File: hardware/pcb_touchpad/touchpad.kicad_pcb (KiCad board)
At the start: 2 copper layers, 41.3 x 30.3 mm, 24 parts, among them U1 IQS9151

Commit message: assigned correct nets to vias
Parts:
- moved U1 32.3 mm to (202.0, 89.7)
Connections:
- net Net-(U1-RX0/TX0) renamed /COL10
- net Net-(U1-RX11/TX11) renamed /ROW13
- net Net-(U1-RX12/TX12) renamed /ROW12
- net Net-(U1-RX1/TX1) renamed /COL9
- net Net-(U1-RX2/TX2) renamed /COL8
- net Net-(U1-RX3/TX3) renamed /COL7
- net Net-(U1-RX4/TX4) renamed /COL6
- net Net-(U1-RX5/TX5) renamed /COL5
- net Net-(U1-RX6/TX6) renamed /COL4
- net Net-(U1-RX7/TX7) renamed /COL3
- net Net-(U1-RX8/TX8) renamed /COL2
- net Net-(U1-RX9/TX9) renamed /COL1
- net Net-(U1-TX33) renamed /ROW11
- net Net-(U1-TX34) renamed /ROW10
- net Net-(U1-TX35) renamed /ROW9
- net Net-(U1-TX36) renamed /ROW8
- net Net-(U1-TX37) renamed /ROW
- net Net-(U1-TX38) renamed /ROW6
- net Net-(U1-TX39) renamed /ROW5
- net Net-(U1-TX40) renamed /ROW4
- net Net-(U1-TX41) renamed /ROW3
- net Net-(U1-TX42) renamed /ROW2
- net Net-(U1-TX43) renamed /ROW1
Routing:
- net (no net): track 141.8 -> 0.00 mm, vias 234 -> 0
- net /COL7: track 0.00 -> 15.8 mm, vias 0 -> 26
- net /COL6: track 0.00 -> 15.8 mm, vias 0 -> 26
- net /COL5: track 0.00 -> 15.8 mm, vias 0 -> 26
- net /COL4: track 0.00 -> 15.8 mm, vias 0 -> 26
- net /COL3: track 0.00 -> 15.8 mm, vias 0 -> 26
- net /COL10: track 0.00 -> 15.8 mm, vias 0 -> 26
- net /COL1: track 0.00 -> 15.8 mm, vias 0 -> 26
- net /COL9: track 1.21 -> 15.8 mm, vias 2 -> 26
- net /COL8: track 1.21 -> 15.8 mm, vias 2 -> 26
- net /COL2: track 1.21 -> 15.8 mm, vias 2 -> 26
- net GND: track 6.06 -> 0.00 mm, vias 10 -> 0
- net /ROW11: track 31.5 -> 29.1 mm, vias 4 -> 0
- net unconnected-(U1-NC-Pad37): track 1.21 -> 0.00 mm, vias 2 -> 0
- net /ROW4: track 30.3 -> 29.1 mm, vias 2 -> 0
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
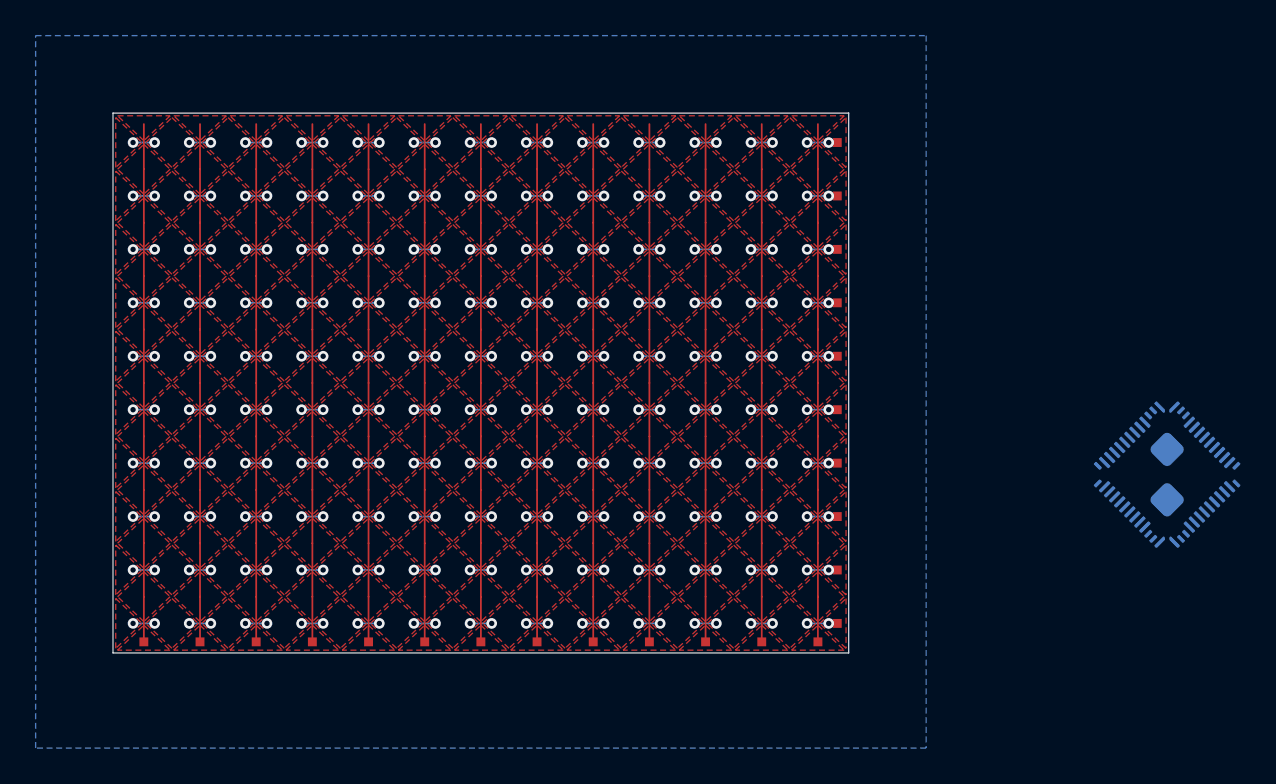
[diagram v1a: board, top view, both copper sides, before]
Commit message: positioned footprint, changed tracks to 0.15mm, moved vias to make drc happy for trackpad
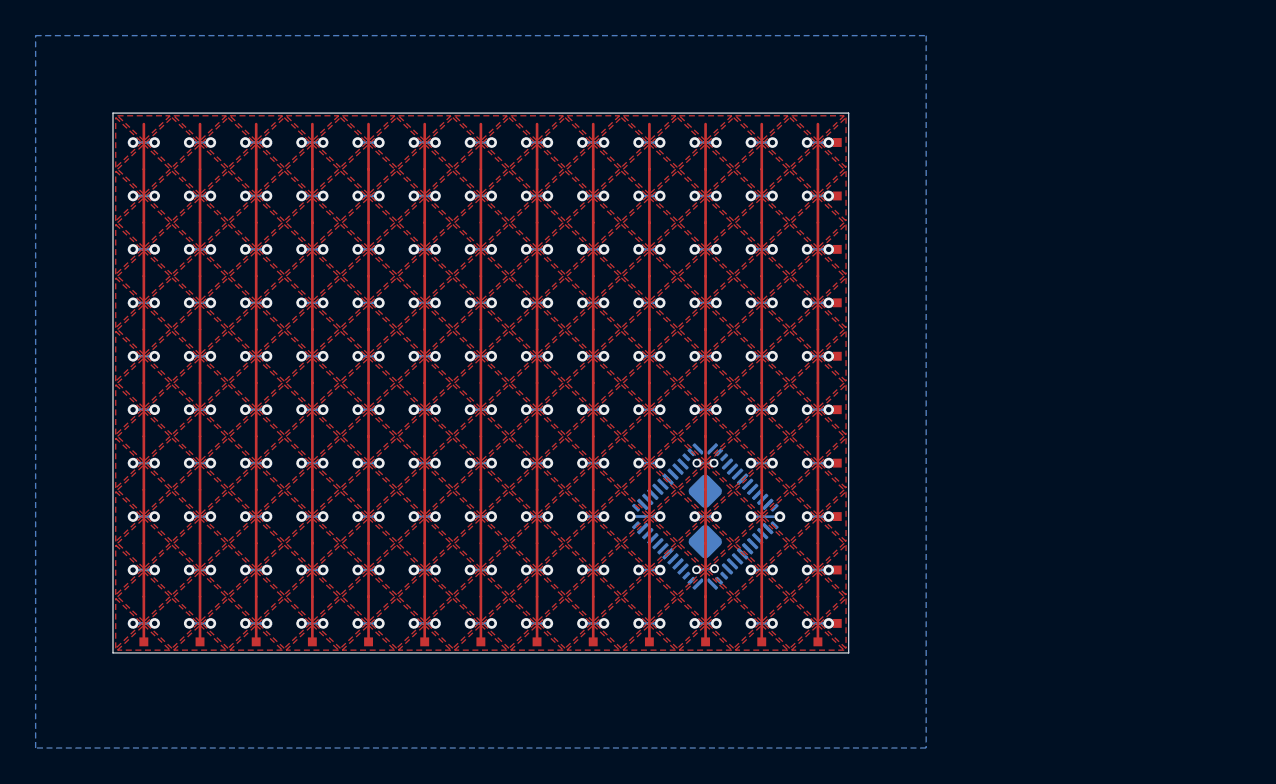
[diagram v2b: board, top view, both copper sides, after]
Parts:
- moved U1 26.0 mm to (176.1, 92.0)
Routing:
- net /COL3: track 15.8 -> 16.6 mm
